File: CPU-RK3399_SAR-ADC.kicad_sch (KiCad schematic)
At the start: 7 parts, among them U1 RK3399

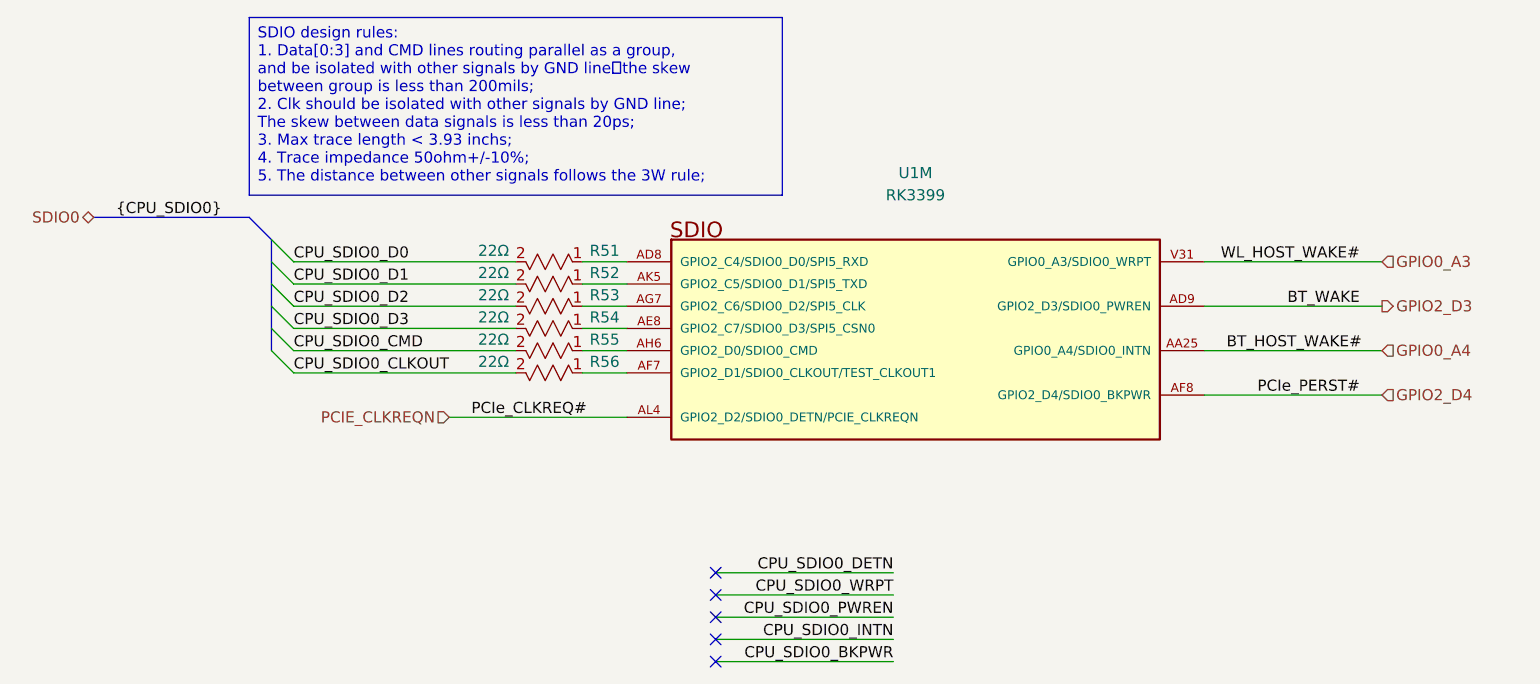
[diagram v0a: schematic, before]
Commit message: update schematic
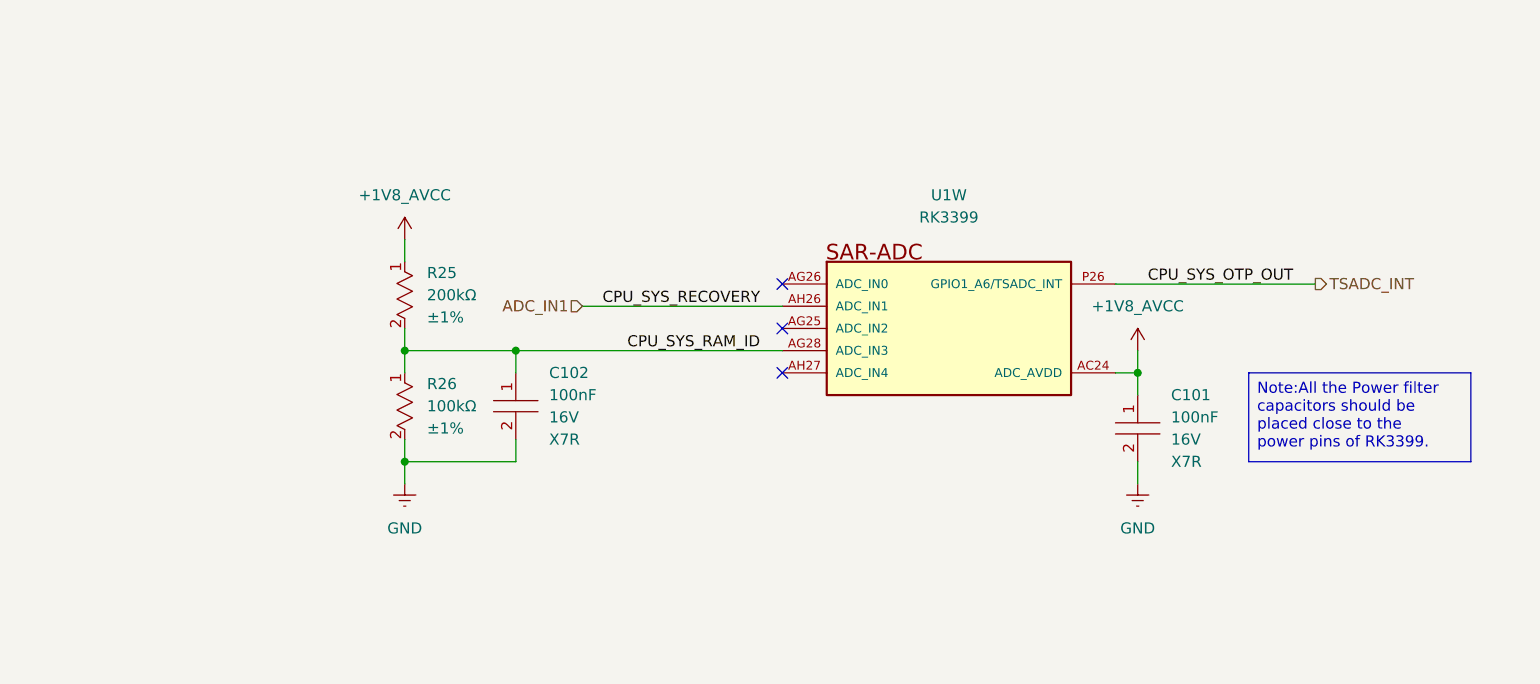
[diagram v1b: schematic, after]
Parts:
- removed R51, R52, R53, R54, R55, R56: ~, footprints:RESC1005X35N, symbol component_library:Resistors/0402WGF220JTCE
- removed U1: RK3399, footprints:BGA828C65P31X31_2100X2100X161, symbol component_library:System On Chip (SoC)/RK3399
- added C101, C102: ~, footprints:CAPC1005X50N, symbol component_library:Capacitors/CL05B104KO5NNNC
- added R25: ~, footprints:RESC1005X35N, symbol component_library:Resistors/0402WGF2003TCE
- added R26: ~, footprints:RESC1005X35N, symbol component_library:Resistors/0402WGF1003TCE
- added U1: RK3399, footprints:BGA828C65P31X31_2100X2100X161, symbol component_library:System On Chip (SoC)/RK3399
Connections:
- new net +1V8_AVCC: C101.1, R25.1, U1.AC24 (ADC_AVDD)
- new net ADC_IN1: U1.AH26 (ADC_IN1)
- new net CPU_SYS_RAM_ID: C102.1, R25.2, R26.1, U1.AG28 (ADC_IN3)
- new net GND: C101.2, C102.2, R26.2
- new net TSADC_INT: U1.P26 (GPIO1_A6/TSADC_INT)
- no-connect marks 5 -> 3
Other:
- title: CPU-RK3399 SDIO Controller -> CPU-RK3399 SAR-ADC Controller

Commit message: update design power
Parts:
- renumbered C102 to C156, C101 to C157, R25 to R48, R26 to R49, U1 to U2
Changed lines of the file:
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@@
 		(on_board yes)
 		(dnp no)
-		(property "Reference" "C101"
+		(property "Reference" "C157"
 			(at 179.07 99.0599 0)
 			(effects
@@
 			(project "VESA-SBC3399"
 				(path "/ebc9dc57-8b05-484a-a5cd-c53b1efc71d3/a7299b18-4123-434b-8c69-0b9524fffa12/8e54df69-c690-4274-be8c-a875e1312d09"
-					(reference "C101")
+					(reference "C157")
 					(unit 1)
 				)
@@
 		(dnp no)
 		(fields_autoplaced yes)
-		(property "Reference" "#PWR0103"
+		(property "Reference" "#PWR0189"
 			(at 91.44 115.57 0)
 			(effects
@@
 			(project "VESA-SBC3399"
 				(path "/ebc9dc57-8b05-484a-a5cd-c53b1efc71d3/a7299b18-4123-434b-8c69-0b9524fffa12/8e54df69-c690-4274-be8c-a875e1312d09"
-					(reference "#PWR0103")
+					(reference "#PWR0189")
 					(unit 1)
 				)
@@
 		(on_board yes)
 		(dnp no)
-		(property "Reference" "C102"
+		(property "Reference" "C156"
 			(at 107.95 96.5199 0)
 			(effects
@@
 			(project ""
 				(path "/ebc9dc57-8b05-484a-a5cd-c53b1efc71d3/a7299b18-4123-434b-8c69-0b9524fffa12/8e54df69-c690-4274-be8c-a875e1312d09"
-					(reference "C102")
+					(reference "C156")
 					(unit 1)
 				)
@@
 		(on_board yes)
 		(dnp no)
-		(property "Reference" "#PWR0101"
+		(property "Reference" "#PWR0188"
 			(at 175.26 97.79 0)
 			(effects
@@
 			(project "VESA-SBC3399"
 				(path "/ebc9dc57-8b05-484a-a5cd-c53b1efc71d3/a7299b18-4123-434b-8c69-0b9524fffa12/8e54df69-c690-4274-be8c-a875e1312d09"
-					(reference "#PWR0101")
+					(reference "#PWR0188")
 					(unit 1)
 				)
@@
 		(on_board yes)
 		(dnp no)
-		(property "Reference" "#PWR0100"
+		(property "Reference" "#PWR0187"
 			(at 91.44 85.09 0)
 			(effects
@@
 			(project "VESA-SBC3399"
 				(path "/ebc9dc57-8b05-484a-a5cd-c53b1efc71d3/a7299b18-4123-434b-8c69-0b9524fffa12/8e54df69-c690-4274-be8c-a875e1312d09"
-					(reference "#PWR0100")
+					(reference "#PWR0187")
 					(unit 1)
 				)
@@
 		(dnp no)
 		(fields_autoplaced yes)
-		(property "Reference" "R26"
+		(property "Reference" "R49"
 			(at 93.98 97.7899 90)
 			(effects
@@
 			(project ""
 				(path "/ebc9dc57-8b05-484a-a5cd-c53b1efc71d3/a7299b18-4123-434b-8c69-0b9524fffa12/8e54df69-c690-4274-be8c-a875e1312d09"
-					(reference "R26")
+					(reference "R49")
 					(unit 1)
 				)
@@
 		(dnp no)
 		(fields_autoplaced yes)
-		(property "Reference" "#PWR0102"
+		(property "Reference" "#PWR0190"
 			(at 175.26 115.57 0)
 			(effects
@@
 			(project "VESA-SBC3399"
 				(path "/ebc9dc57-8b05-484a-a5cd-c53b1efc71d3/a7299b18-4123-434b-8c69-0b9524fffa12/8e54df69-c690-4274-be8c-a875e1312d09"
-					(reference "#PWR0102")
+					(reference "#PWR0190")
 					(unit 1)
 				)
@@
 		(dnp no)
 		(fields_autoplaced yes)
-		(property "Reference" "U1"
+		(property "Reference" "U2"
 			(at 153.67 76.2 0)
 			(effects
@@
 			(project ""
 				(path "/ebc9dc57-8b05-484a-a5cd-c53b1efc71d3/a7299b18-4123-434b-8c69-0b9524fffa12/8e54df69-c690-4274-be8c-a875e1312d09"
-					(reference "U1")
+					(reference "U2")
 					(unit 23)
 				)
@@
 		(dnp no)
 		(fields_autoplaced yes)
-		(property "Reference" "R25"
+		(property "Reference" "R48"
 			(at 93.98 85.0899 90)
 			(effects
@@
 			(project ""
 				(path "/ebc9dc57-8b05-484a-a5cd-c53b1efc71d3/a7299b18-4123-434b-8c69-0b9524fffa12/8e54df69-c690-4274-be8c-a875e1312d09"
-					(reference "R25")
+					(reference "R48")
 					(unit 1)
 				)

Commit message: design DDR
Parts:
- renumbered C156 to C283, C157 to C284, R48 to R119, R49 to R120, U2 to U17
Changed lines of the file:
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@@
 		(on_board yes)
 		(dnp no)
-		(property "Reference" "C157"
+		(property "Reference" "C284"
 			(at 179.07 99.0599 0)
 			(effects
@@
 			(project "VESA-SBC3399"
 				(path "/ebc9dc57-8b05-484a-a5cd-c53b1efc71d3/a7299b18-4123-434b-8c69-0b9524fffa12/8e54df69-c690-4274-be8c-a875e1312d09"
-					(reference "C157")
+					(reference "C284")
 					(unit 1)
 				)
@@
 		(dnp no)
 		(fields_autoplaced yes)
-		(property "Reference" "#PWR0189"
+		(property "Reference" "#PWR0349"
 			(at 91.44 115.57 0)
 			(effects
@@
 			(project "VESA-SBC3399"
 				(path "/ebc9dc57-8b05-484a-a5cd-c53b1efc71d3/a7299b18-4123-434b-8c69-0b9524fffa12/8e54df69-c690-4274-be8c-a875e1312d09"
-					(reference "#PWR0189")
+					(reference "#PWR0349")
 					(unit 1)
 				)
@@
 		(on_board yes)
 		(dnp no)
-		(property "Reference" "C156"
+		(property "Reference" "C283"
 			(at 107.95 96.5199 0)
 			(effects
@@
 			(project ""
 				(path "/ebc9dc57-8b05-484a-a5cd-c53b1efc71d3/a7299b18-4123-434b-8c69-0b9524fffa12/8e54df69-c690-4274-be8c-a875e1312d09"
-					(reference "C156")
+					(reference "C283")
 					(unit 1)
 				)
@@
 		(on_board yes)
 		(dnp no)
-		(property "Reference" "#PWR0188"
+		(property "Reference" "#PWR0348"
 			(at 175.26 97.79 0)
 			(effects
@@
 			(project "VESA-SBC3399"
 				(path "/ebc9dc57-8b05-484a-a5cd-c53b1efc71d3/a7299b18-4123-434b-8c69-0b9524fffa12/8e54df69-c690-4274-be8c-a875e1312d09"
-					(reference "#PWR0188")
+					(reference "#PWR0348")
 					(unit 1)
 				)
@@
 		(on_board yes)
 		(dnp no)
-		(property "Reference" "#PWR0187"
+		(property "Reference" "#PWR0347"
 			(at 91.44 85.09 0)
 			(effects
@@
 			(project "VESA-SBC3399"
 				(path "/ebc9dc57-8b05-484a-a5cd-c53b1efc71d3/a7299b18-4123-434b-8c69-0b9524fffa12/8e54df69-c690-4274-be8c-a875e1312d09"
-					(reference "#PWR0187")
+					(reference "#PWR0347")
 					(unit 1)
 				)
@@
 		(dnp no)
 		(fields_autoplaced yes)
-		(property "Reference" "R49"
+		(property "Reference" "R120"
 			(at 93.98 97.7899 90)
 			(effects
@@
 			(project ""
 				(path "/ebc9dc57-8b05-484a-a5cd-c53b1efc71d3/a7299b18-4123-434b-8c69-0b9524fffa12/8e54df69-c690-4274-be8c-a875e1312d09"
-					(reference "R49")
+					(reference "R120")
 					(unit 1)
 				)
@@
 		(dnp no)
 		(fields_autoplaced yes)
-		(property "Reference" "#PWR0190"
+		(property "Reference" "#PWR0350"
 			(at 175.26 115.57 0)
 			(effects
@@
 			(project "VESA-SBC3399"
 				(path "/ebc9dc57-8b05-484a-a5cd-c53b1efc71d3/a7299b18-4123-434b-8c69-0b9524fffa12/8e54df69-c690-4274-be8c-a875e1312d09"
-					(reference "#PWR0190")
+					(reference "#PWR0350")
 					(unit 1)
 				)
@@
 		(dnp no)
 		(fields_autoplaced yes)
-		(property "Reference" "U2"
+		(property "Reference" "U17"
 			(at 153.67 76.2 0)
 			(effects
@@
 		)
 		(property "Footprint" "footprints:BGA828C65P31X31_2100X2100X161"
-			(at 154.94 96.52 0)
+			(at 152.4 96.52 0)
 			(effects
 				(font
@@
 			(project ""
 				(path "/ebc9dc57-8b05-484a-a5cd-c53b1efc71d3/a7299b18-4123-434b-8c69-0b9524fffa12/8e54df69-c690-4274-be8c-a875e1312d09"
-					(reference "U2")
+					(reference "U17")
 					(unit 23)
 				)
@@
 		(dnp no)
 		(fields_autoplaced yes)
-		(property "Reference" "R48"
+		(property "Reference" "R119"
 			(at 93.98 85.0899 90)
 			(effects
@@
 			(project ""
 				(path "/ebc9dc57-8b05-484a-a5cd-c53b1efc71d3/a7299b18-4123-434b-8c69-0b9524fffa12/8e54df69-c690-4274-be8c-a875e1312d09"
-					(reference "R48")
+					(reference "R119")
 					(unit 1)
 				)
